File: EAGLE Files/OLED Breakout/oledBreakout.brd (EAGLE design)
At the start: 100 x 80 mm, 1 part

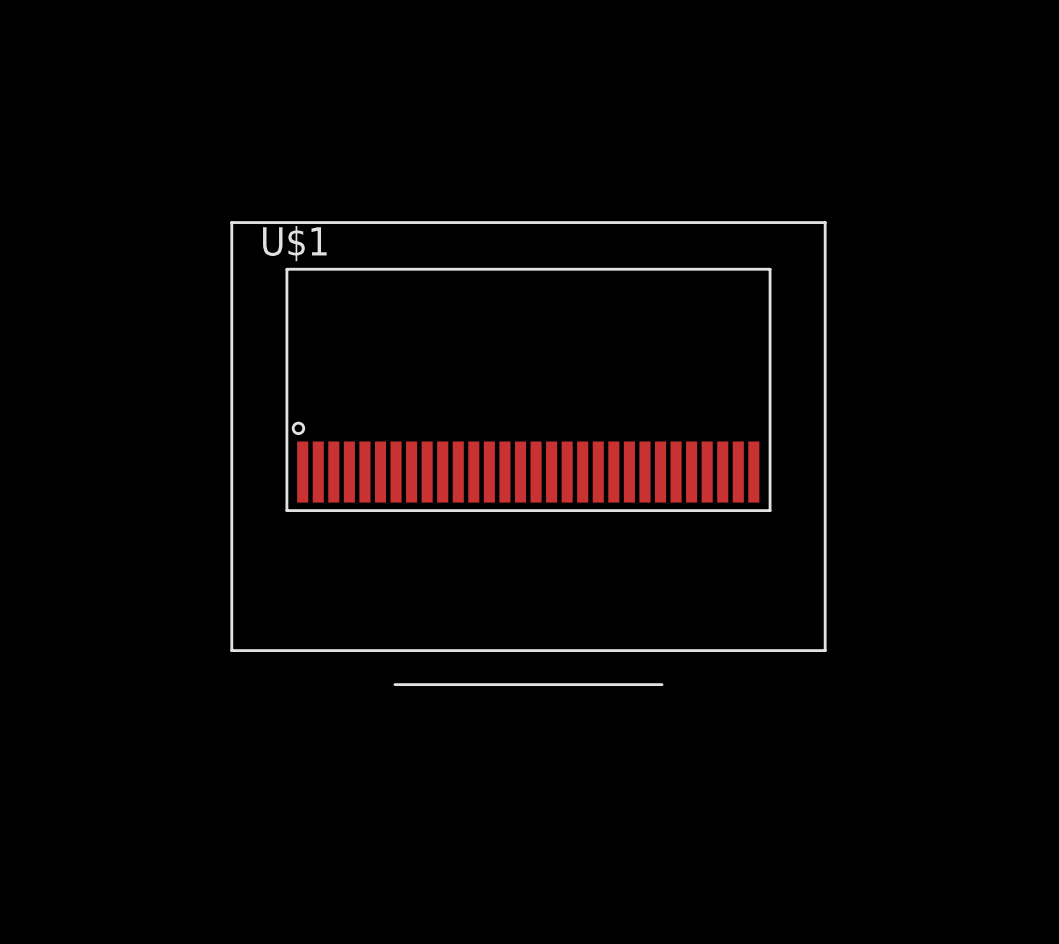
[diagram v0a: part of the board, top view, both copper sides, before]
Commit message: OLED breakout mostly finished. Need to merge with power breakout and decide on header/outputs.
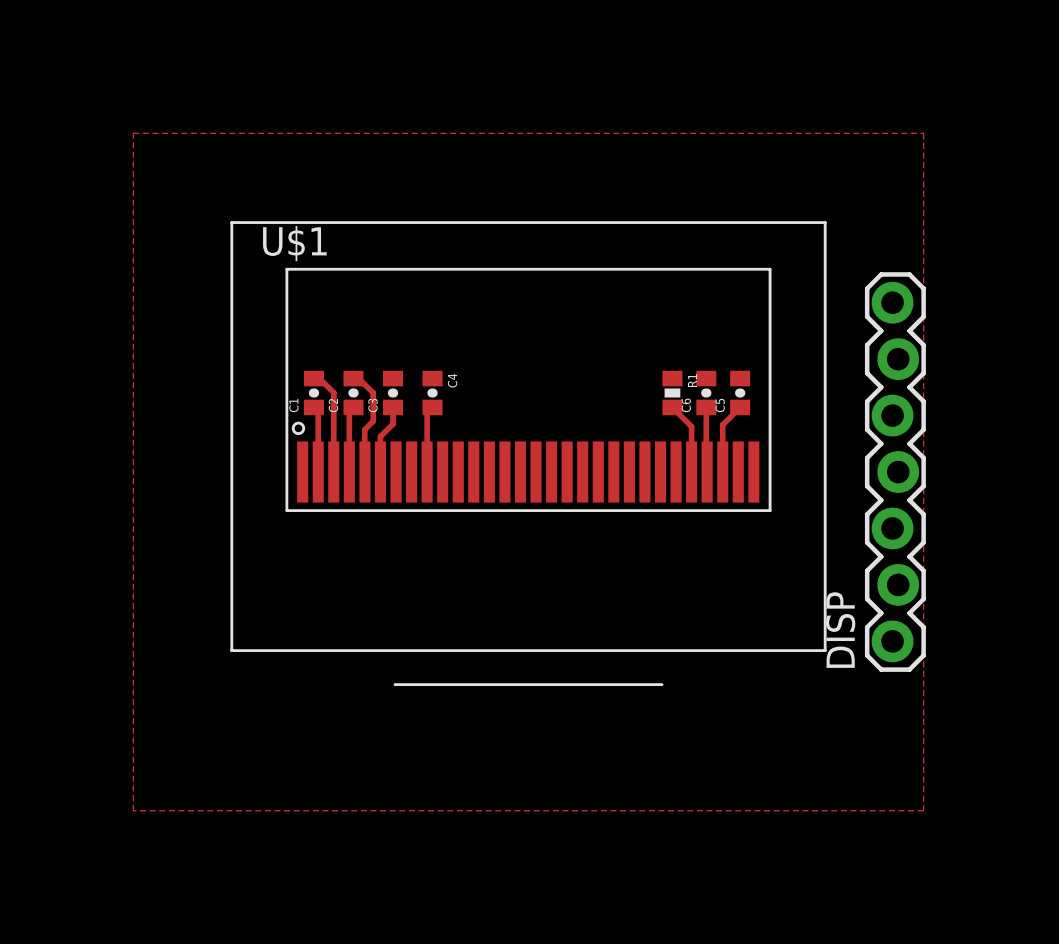
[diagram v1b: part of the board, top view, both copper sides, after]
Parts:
- added C1, C2, C3, C4: 1uF, chips:0402-CAP
- added C5: 2.2uF, chips:0402-CAP
- added C6: 4.7uF, chips:0402-CAP
- added DISP: (no value), SparkFun-Connectors:1X07_LOCK
- added R1: 390K, chips:0402-RES
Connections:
- removed net CAP1N: U$1.5
- removed net CAP1P: U$1.4
- removed net CAP2N: U$1.3
- removed net CAP2P: U$1.2
- removed net IREF: U$1.26
- removed net VBAT: U$1.6
- removed net VCC: U$1.28
- removed net VCOMH: U$1.27
- removed net VDD: U$1.9
- removed net VLSS: U$1.29
- removed net VSS: U$1.1, U$1.30, U$1.8
- new net 3.3V: C4.2, U$1.9
- new net 3.6V: C3.1, U$1.6
- new net C/D#: DISP.3, U$1.15
- new net CS#: DISP.4, U$1.13
- new net GND: C3.2, C4.1, C5.2, C6.2, DISP.7, R1.1, U$1.1, U$1.10, U$1.11, U$1.12, U$1.16, U$1.17, U$1.21, U$1.22, U$1.23, U$1.24, U$1.25, U$1.29, U$1.30, U$1.8
- new net MOSI: DISP.1, U$1.19
- new net N$10: C2.1, U$1.4
- new net N$11: C1.2, U$1.3
- new net N$12: C1.1, U$1.2
- new net N$2: C5.1, U$1.28
- new net N$3: C6.1, U$1.27
- new net N$4: R1.2, U$1.26
- new net N$9: C2.2, U$1.5
- new net RESET: DISP.5, U$1.14
- new net SCK: DISP.2, U$1.18
- new net VBAT_EN: DISP.6
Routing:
- net N$9: track 0.00 -> 4.90 mm
- net N$11: track 0.00 -> 4.72 mm
- net N$4: track 0.00 -> 3.26 mm
- net N$2: track 0.00 -> 3.23 mm
- net 3.6V: track 0.00 -> 3.14 mm
- net 3.3V: track 0.00 -> 3.06 mm
- net N$12: track 0.00 -> 2.99 mm
- net N$10: track 0.00 -> 2.98 mm
- net N$3: track 0.00 -> 2.92 mm
- added copper zone on layer 1, net GND

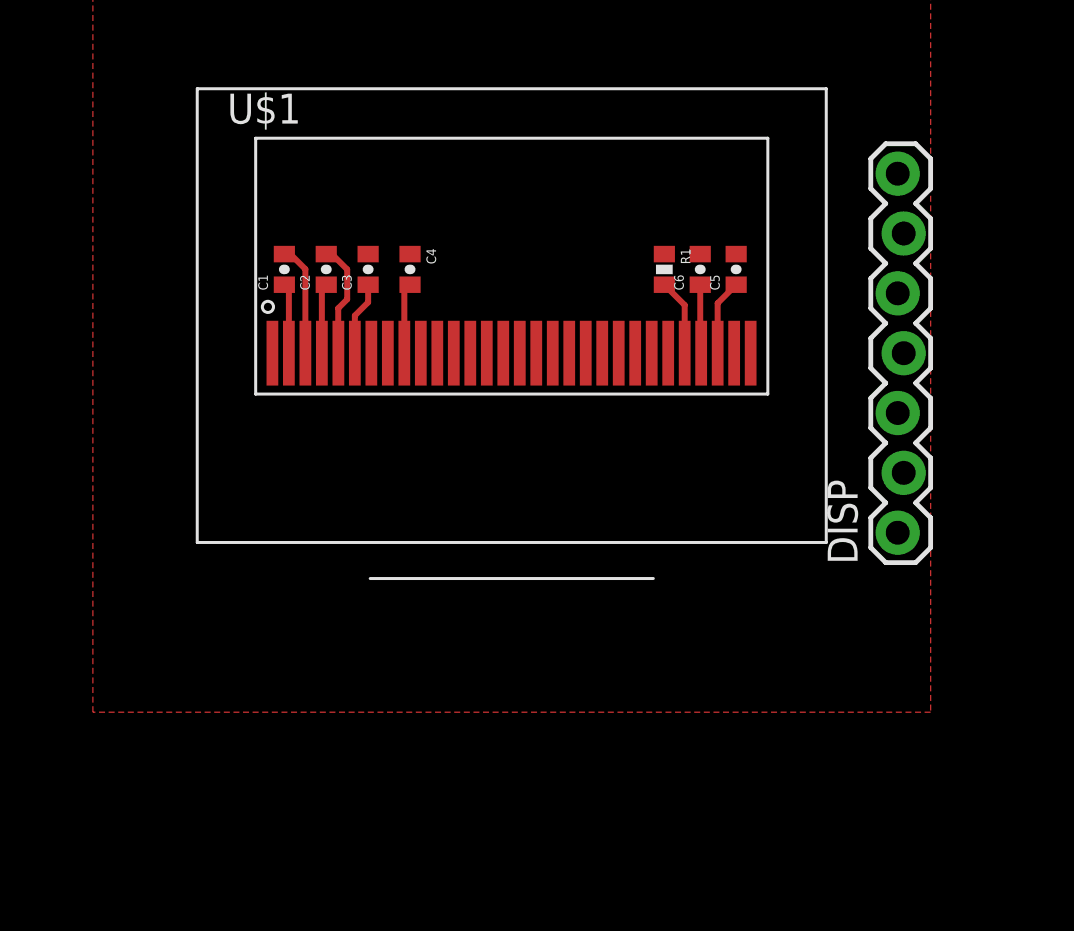
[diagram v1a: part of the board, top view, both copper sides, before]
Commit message: Combined power/OLED breakouts. Not yet routed completely.
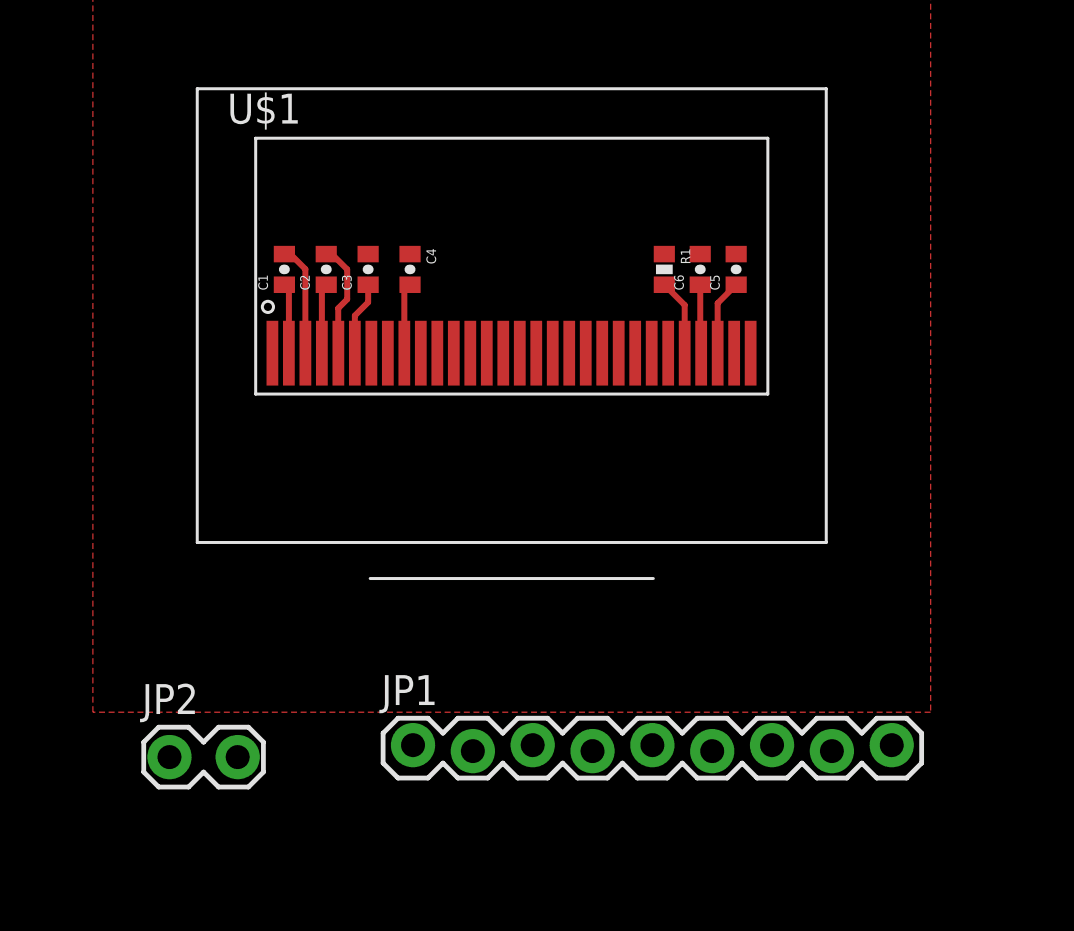
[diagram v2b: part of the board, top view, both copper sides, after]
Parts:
- removed DISP: (no value), SparkFun-Connectors:1X07_LOCK
- added JP1: M09LOCK, SparkFun-Connectors:1X09_LOCK
- added JP2: M02LOCK, SparkFun-Connectors:1X02_LOCK
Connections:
- removed net VBAT_EN: DISP.6
- new net PWR_DN: JP1.4
- new net VIN: JP2.2
- net 3.3V: now also JP1.2
- net 3.6V: now also JP1.3
- net C/D#: now also JP1.7; no longer DISP.3
- net CS#: now also JP1.6; no longer DISP.4
- net GND: now also JP1.1, JP2.1; no longer DISP.7
- net MOSI: now also JP1.9; no longer DISP.1
- net RESET: now also JP1.5; no longer DISP.5
- net SCK: now also JP1.8; no longer DISP.2
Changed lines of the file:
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@@
 <element name="C6" library="chips" package="0402-CAP" value="4.7uF" x="56.261" y="41.656" rot="R90"/>
 <element name="R1" library="chips" package="0402-RES" value="390K" x="54.737" y="41.656" rot="R270"/>
-<element name="DISP" library="SparkFun-Connectors" package="1X07_LOCK" value="" x="64.77" y="30.48" rot="R90"/>
+<element name="JP1" library="SparkFun-Connectors" package="1X09_LOCK" value="M09LOCK" x="44.069" y="21.336"/>
+<element name="JP2" library="SparkFun-Connectors" package="1X02_LOCK" value="M02LOCK" x="33.909" y="20.955"/>
 </elements>
 <signals>
@@
 <vertex x="30.48" y="22.86"/>
 </polygon>
-<contactref element="DISP" pad="7"/>
-<wire x1="38.1" y1="38.1" x2="64.643" y2="45.72" width="0" layer="19" extent="1-1"/>
+<contactref element="JP1" pad="1"/>
+<contactref element="JP2" pad="1"/>
+<wire x1="56.261" y1="42.306" x2="57.785" y2="42.306" width="0" layer="19" extent="1-1"/>
+<wire x1="54.737" y1="42.306" x2="56.261" y2="42.306" width="0" layer="19" extent="1-1"/>
+<wire x1="57.7" y1="38.1" x2="57.785" y2="42.306" width="0" layer="19" extent="1-1"/>
+<wire x1="58.4" y1="38.1" x2="57.7" y2="38.1" width="0" layer="19" extent="1-1"/>
+<wire x1="54.9" y1="38.1" x2="57.7" y2="38.1" width="0" layer="19" extent="1-1"/>
+<wire x1="54.2" y1="38.1" x2="54.9" y2="38.1" width="0" layer="19" extent="1-1"/>
+<wire x1="53.5" y1="38.1" x2="54.2" y2="38.1" width="0" layer="19" extent="1-1"/>
+<wire x1="52.8" y1="38.1" x2="53.5" y2="38.1" width="0" layer="19" extent="1-1"/>
+<wire x1="52.1" y1="38.1" x2="52.8" y2="38.1" width="0" layer="19" extent="1-1"/>
+<wire x1="49.3" y1="38.1" x2="52.1" y2="38.1" width="0" layer="19" extent="1-1"/>
+<wire x1="48.6" y1="38.1" x2="49.3" y2="38.1" width="0" layer="19" extent="1-1"/>
+<wire x1="45.8" y1="38.1" x2="48.6" y2="38.1" width="0" layer="19" extent="1-1"/>
+<wire x1="45.1" y1="38.1" x2="45.8" y2="38.1" width="0" layer="19" extent="1-1"/>
+<wire x1="44.4" y1="38.1" x2="45.1" y2="38.1" width="0" layer="19" extent="1-1"/>
+<wire x1="43" y1="38.1" x2="44.4" y2="38.1" width="0" layer="19" extent="1-1"/>
+<wire x1="43.942" y1="42.306" x2="44.4" y2="38.1" width="0" layer="19" extent="1-1"/>
+<wire x1="42.164" y1="42.306" x2="43.942" y2="42.306" width="0" layer="19" extent="1-1"/>
+<wire x1="38.1" y1="38.1" x2="43" y2="38.1" width="0" layer="19" extent="1-1"/>
+<wire x1="44.069" y1="21.463" x2="44.4" y2="38.1" width="0" layer="19" extent="1-1"/>
+<wire x1="33.7312" y1="20.955" x2="44.069" y2="21.463" width="0" layer="19" extent="1-1"/>
 </signal>
 <signal name="N$2">
@@
 <wire x1="42.164" y1="40.259" x2="41.6" y2="39.695" width="0.254" layer="1"/>
 <wire x1="41.6" y1="39.695" x2="41.6" y2="38.1" width="0.254" layer="1"/>
+<contactref element="JP1" pad="3"/>
+<wire x1="49.149" y1="21.463" x2="41.6" y2="38.1" width="0" layer="19" extent="1-1"/>
 </signal>
 <signal name="3.3V">
@@
 <wire x1="43.942" y1="41.006" x2="43.7" y2="40.891" width="0.254" layer="1"/>
 <wire x1="43.7" y1="40.891" x2="43.7" y2="38.1" width="0.254" layer="1"/>
+<contactref element="JP1" pad="2"/>
+<wire x1="46.609" y1="21.209" x2="43.7" y2="38.1" width="0" layer="19" extent="1-1"/>
 </signal>
 <signal name="N$9">
@@
 <signal name="CS#">
 <contactref element="U$1" pad="13"/>
-<contactref element="DISP" pad="4"/>
-<wire x1="64.897" y1="38.1" x2="46.5" y2="38.1" width="0" layer="19" extent="1-1"/>
+<contactref element="JP1" pad="6"/>
+<wire x1="56.769" y1="21.209" x2="46.5" y2="38.1" width="0" layer="19" extent="1-1"/>
 </signal>
 <signal name="RESET">
 <contactref element="U$1" pad="14"/>
-<contactref element="DISP" pad="5"/>
-<wire x1="64.643" y1="40.64" x2="47.2" y2="38.1" width="0" layer="19" extent="1-1"/>
+<contactref element="JP1" pad="5"/>
+<wire x1="54.229" y1="21.463" x2="47.2" y2="38.1" width="0" layer="19" extent="1-1"/>
 </signal>
 <signal name="C/D#">
 <contactref element="U$1" pad="15"/>
-<contactref element="DISP" pad="3"/>
-<wire x1="64.643" y1="35.56" x2="47.9" y2="38.1" width="0" layer="19" extent="1-1"/>
+<contactref element="JP1" pad="7"/>
+<wire x1="59.309" y1="21.463" x2="47.9" y2="38.1" width="0" layer="19" extent="1-1"/>
 </signal>
 <signal name="SCK">
 <contactref element="U$1" pad="18"/>
-<contactref element="DISP" pad="2"/>
-<wire x1="64.897" y1="33.02" x2="50" y2="38.1" width="0" layer="19" extent="1-1"/>
+<contactref element="JP1" pad="8"/>
+<wire x1="61.849" y1="21.209" x2="50" y2="38.1" width="0" layer="19" extent="1-1"/>
 </signal>
 <signal name="MOSI">
 <contactref element="U$1" pad="19"/>
-<contactref element="DISP" pad="1"/>
-<wire x1="64.643" y1="30.48" x2="50.7" y2="38.1" width="0" layer="19" extent="1-1"/>
+<contactref element="JP1" pad="9"/>
+<wire x1="64.389" y1="21.463" x2="50.7" y2="38.1" width="0" layer="19" extent="1-1"/>
 </signal>
-<signal name="VBAT_EN">
-<contactref element="DISP" pad="6"/>
+<signal name="PWR_DN">
+<contactref element="JP1" pad="4"/>
+</signal>
+<signal name="VIN">
+<contactref element="JP2" pad="2"/>
 </signal>
 </signals>
